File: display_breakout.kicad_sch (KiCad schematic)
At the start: 24 parts, among them J1 Conn_01x06, U1 MP3216GJE-P, U2 CFAL128128A0-015Y

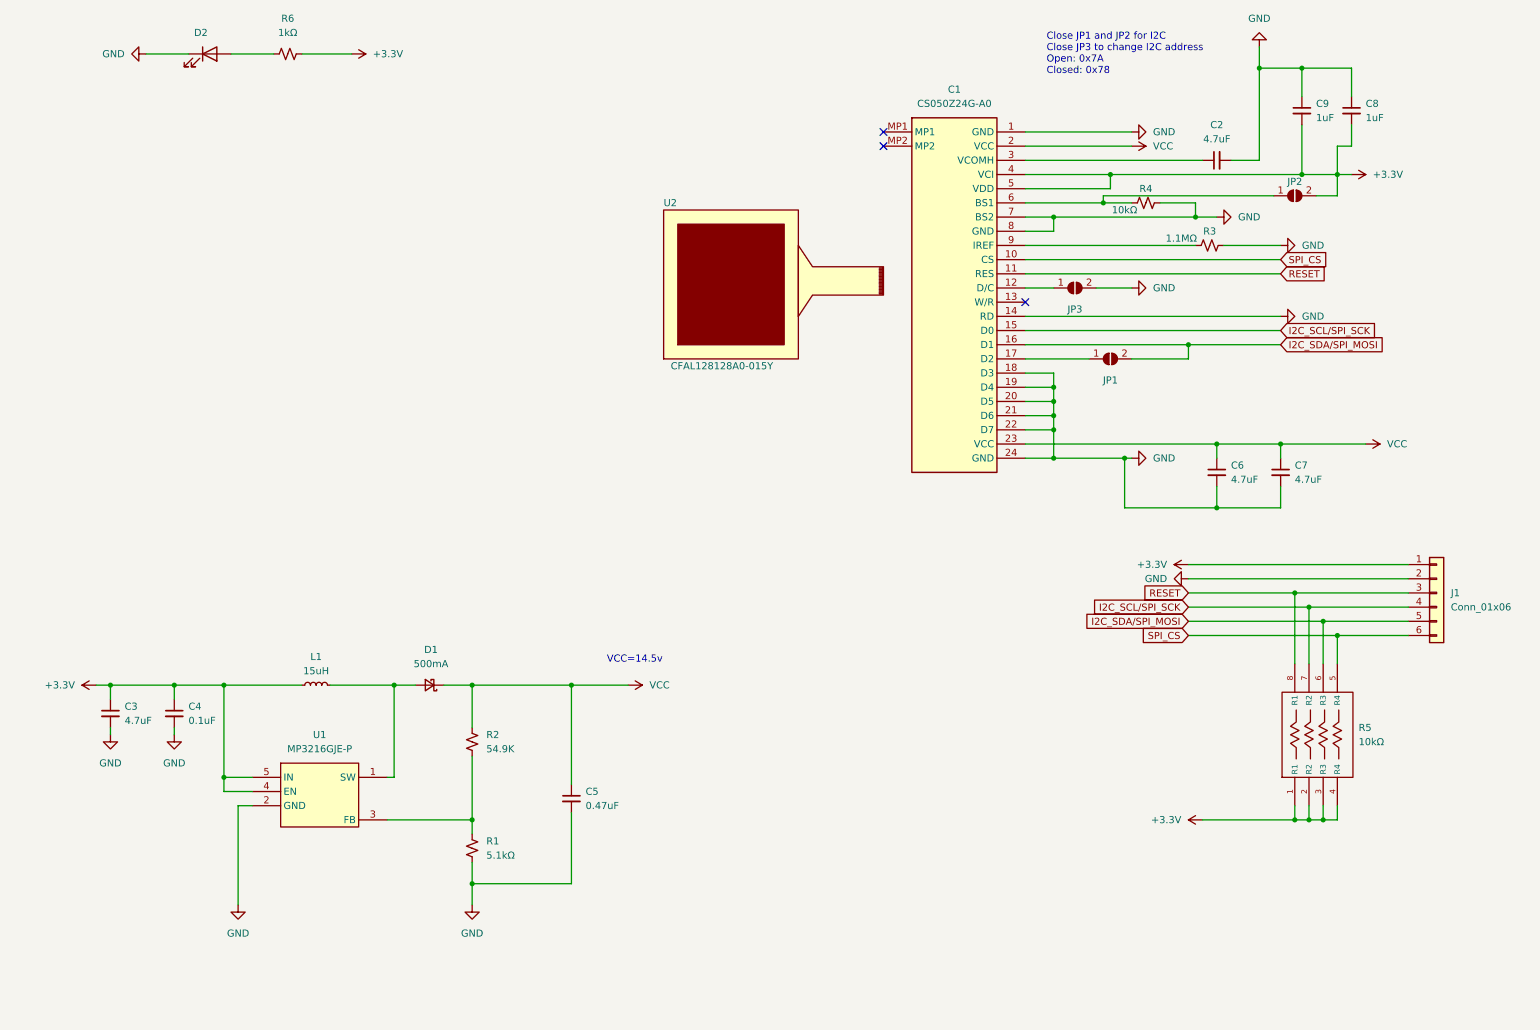
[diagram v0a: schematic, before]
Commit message: Fix backward display footprint, reroute everything
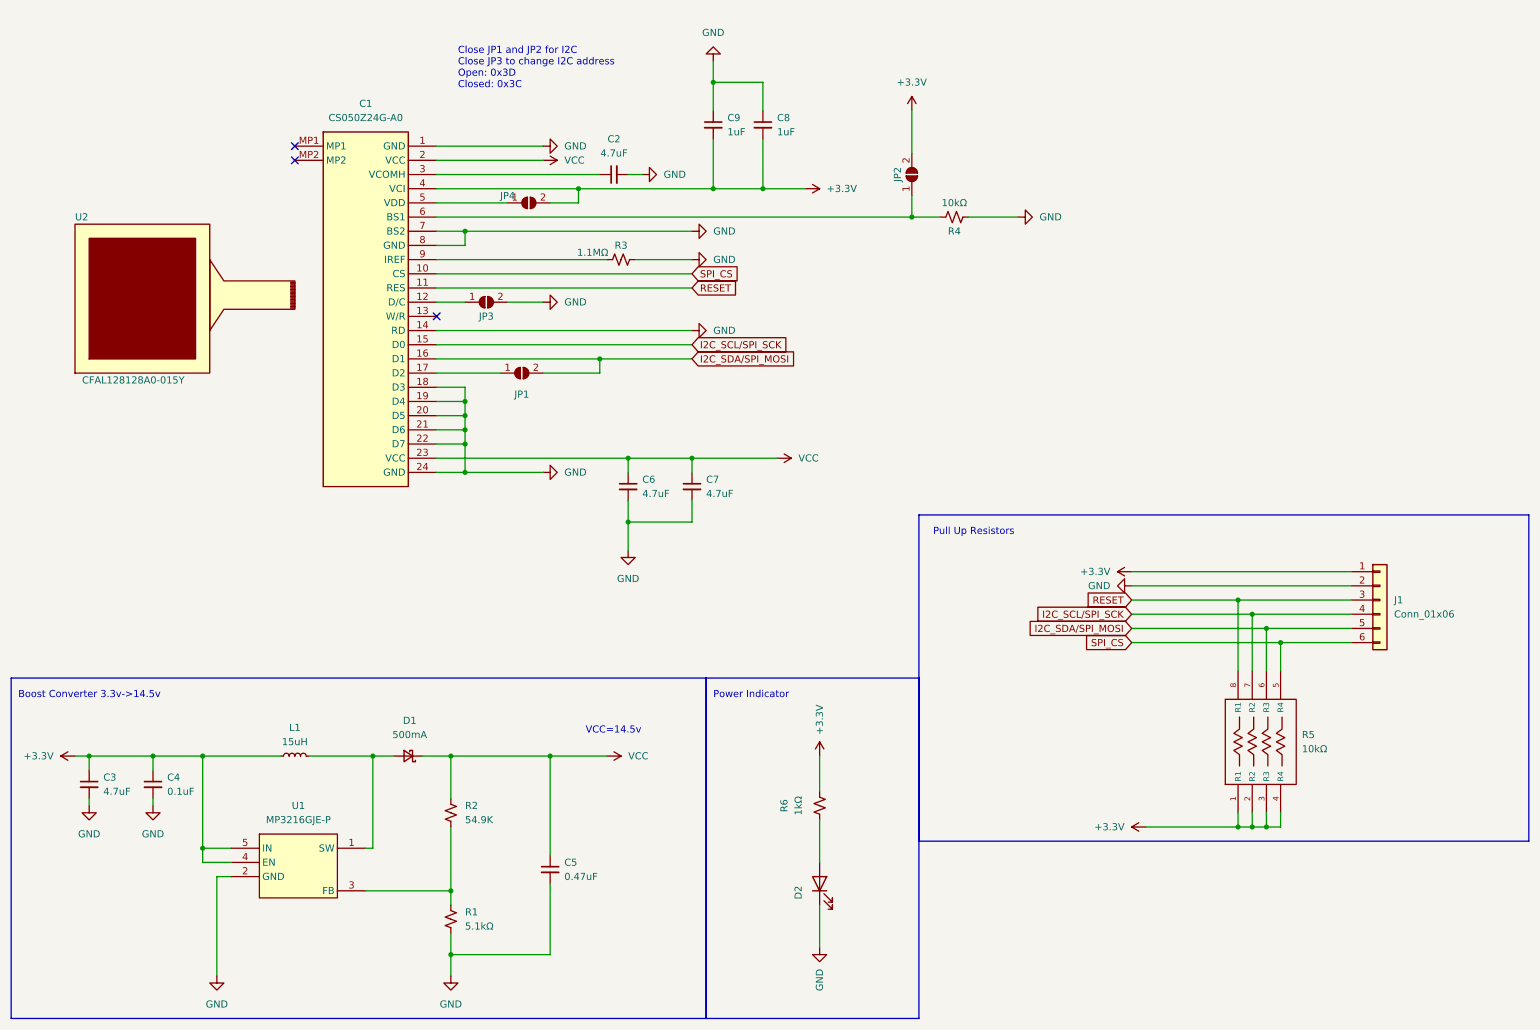
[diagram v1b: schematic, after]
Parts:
- added JP4: SolderJumper_2_Open, Jumper:SolderJumper-2_P1.3mm_Open_RoundedPad1.0x1.5mm, symbol Jumper:SolderJumper_2_Open
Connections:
- net +3.3V: now also JP4.2 (B); no longer C1.5 (VDD)
- net GND: now also R4.1; no longer R4.2
- net at C1.6 (BS1), JP2.1 (A): now also R4.2; no longer R4.1
- new net: C1.5 (VDD), JP4.1 (A)
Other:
- note added: "Boost Converter 3.3v->14.5v"
- note added: "Close JP1 and JP2 for I2C Close JP3 to change I2C address Open: 0x3D Closed: 0x3C"
- note added: "Power Indicator"
- note added: "Pull Up Resistors"
- note removed: "Close JP1 and JP2 for I2C Close JP3 to change I2C address Open: 0x7A Closed: 0x78"
- moved on the sheet: C1, C2, C3, C4, C5, C6, C7, C8, C9, D1, D2, J1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
